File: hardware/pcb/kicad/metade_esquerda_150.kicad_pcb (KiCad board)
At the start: 2 copper layers, 125.4 x 120.5 mm, 177 parts

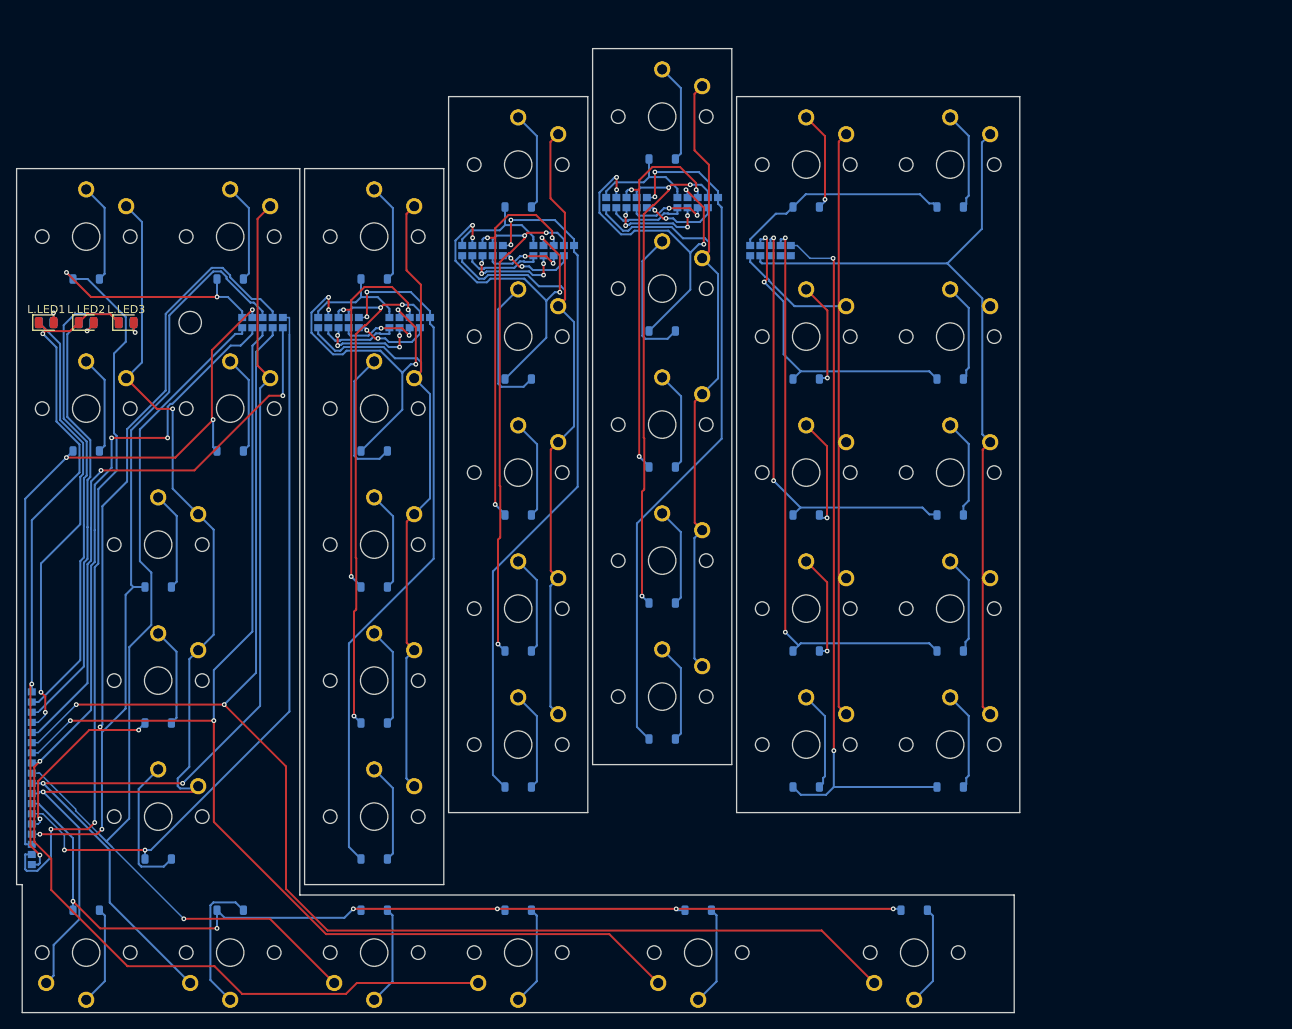
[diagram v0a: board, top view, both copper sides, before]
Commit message: Metade esquerda: placas afastadas 8 mm para ver onde cada uma acaba
Co-Authored-By: Claude Opus 5.5 <noreply@anthropic.com>
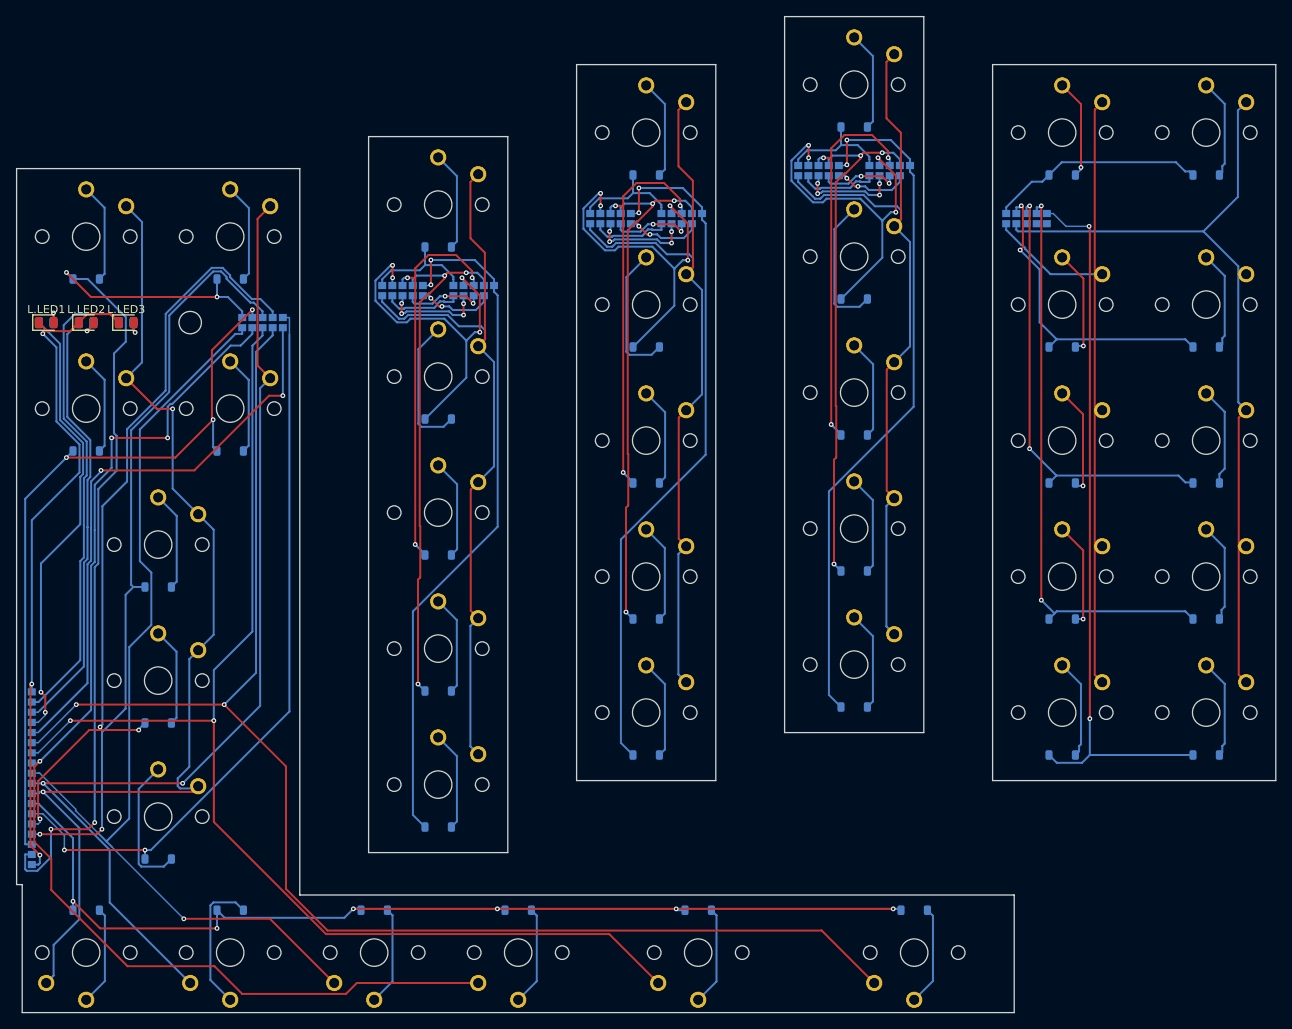
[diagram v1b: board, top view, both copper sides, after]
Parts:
- moved IN.PAD3 32.2 mm to (273.5, 100.6)
- moved IN.PAD8 32.2 mm to (273.5, 101.9)
- moved IN.D1 32.2 mm to (278.0, 168.3)
- moved IN.D10 32.2 mm to (296.0, 95.8)
- moved IN.D2 32.2 mm to (278.0, 151.3)
- moved IN.D3 32.2 mm to (278.0, 134.3)
- moved IN.D4 32.2 mm to (278.0, 117.3)
- moved IN.D5 32.2 mm to (278.0, 95.8)
- moved IN.D6 32.2 mm to (296.0, 168.3)
- moved IN.D7 32.2 mm to (296.0, 151.3)
- moved IN.D8 32.2 mm to (296.0, 134.3)
- moved IN.D9 32.2 mm to (296.0, 117.3)
- moved IN.PAD1 32.2 mm to (271.0, 100.6)
- moved IN.PAD4 32.2 mm to (274.8, 100.6)
- moved IN.PAD6 32.2 mm to (271.0, 101.9)
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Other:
- board size 125.4 x 120.5 mm -> 157.4 x 124.5 mm
